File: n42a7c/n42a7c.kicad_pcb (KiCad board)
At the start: 2 copper layers, 265.5 x 105.1 mm, 111 parts, among them J1 Conn_01x02_Pin, J2 Conn_01x02_Pin, SW1 CPG151101S11-16, SW10 CPG151101S11-16, SW11 CPG151101S11-16, SW12 CPG151101S11-16, SW13 CPG151101S11-16, SW14 CPG151101S11-16, SW15 CPG151101S11-16, SW16 CPG151101S11-16, SW17 CPG151101S11-16, SW18 CPG151101S11-16, SW19 CPG151101S11-16, SW2 CPG151101S11-16, SW20 CPG151101S11-16, SW21 CPG151101S11-16, SW22 CPG151101S11-16, SW23 CPG151101S11-16, SW24 CPG151101S11-16, SW25 CPG151101S11-16, SW26 CPG151101S11-16, SW27 CPG151101S11-16, SW28 CPG151101S11-16, SW29 CPG151101S11-16, SW3 CPG151101S11-16, SW30 CPG151101S11-16, SW31 CPG151101S11-16, SW32 CPG151101S11-16, SW33 CPG151101S11-16, SW34 CPG151101S11-16, SW35 CPG151101S11-16, SW36 CPG151101S11-16, SW37 CPG151101S11-16, SW38 CPG151101S11-16, SW39 CPG151101S11-16, SW4 CPG151101S11-16, SW40 CPG151101S11-16, SW41 CPG151101S11-16, SW42 CPG151101S11-16, SW5 CPG151101S11-16, SW6 CPG151101S11-16, SW7 CPG151101S11-16, SW8 CPG151101S11-16, SW9 CPG151101S11-16, U1 XIAO-nRF52840-SMD

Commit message: revise switch pos.
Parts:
- moved SW_HPWR1 4.80 mm to (192.6, 24.4)
- moved SW_HPWR2 4.80 mm to (192.6, 24.4)
- moved J2 3.12 mm to (183.4, 31.6)
- moved SW_SPWR1 2.99 mm to (182.2, 27.1)
- moved DI4 1.19 mm to (270.3, 69.1)
- moved DS2 1.19 mm to (270.3, 42.9)
- moved DS4 1.19 mm to (270.3, 61.9)
- moved DI2 1.19 mm to (270.3, 50.0)
- moved J1 0.30 mm to (183.4, 38.8)
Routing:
- net Net-(J1-Pin_1): track 34.4 -> 43.6 mm
- net BAT+: track 61.5 -> 65.0 mm
- net IO 7: track 356.1 -> 353.7 mm
- net PWR: track 20.8 -> 22.4 mm
- net BAT-: track 45.6 -> 47.0 mm
- net IO 6: track 361.7 -> 360.5 mm
- net Net-(D19-K): track 107.9 -> 106.7 mm
- net Net-(D10-K): track 115.4 -> 114.2 mm
- net IO 5: track 386.6 -> 385.6 mm
- net IO 3: track 297.5 -> 296.7 mm
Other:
- outline, holes or cut-outs redrawn

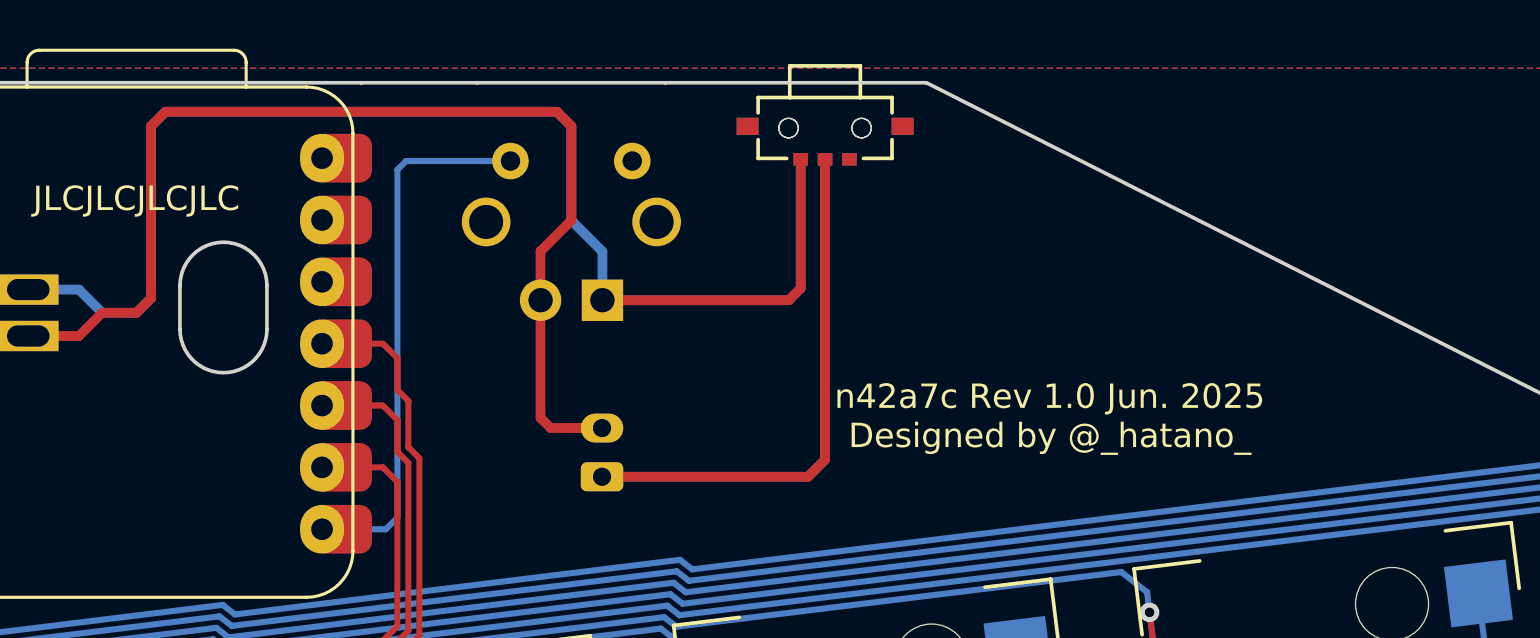
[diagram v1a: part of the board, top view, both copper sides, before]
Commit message: revise power connector
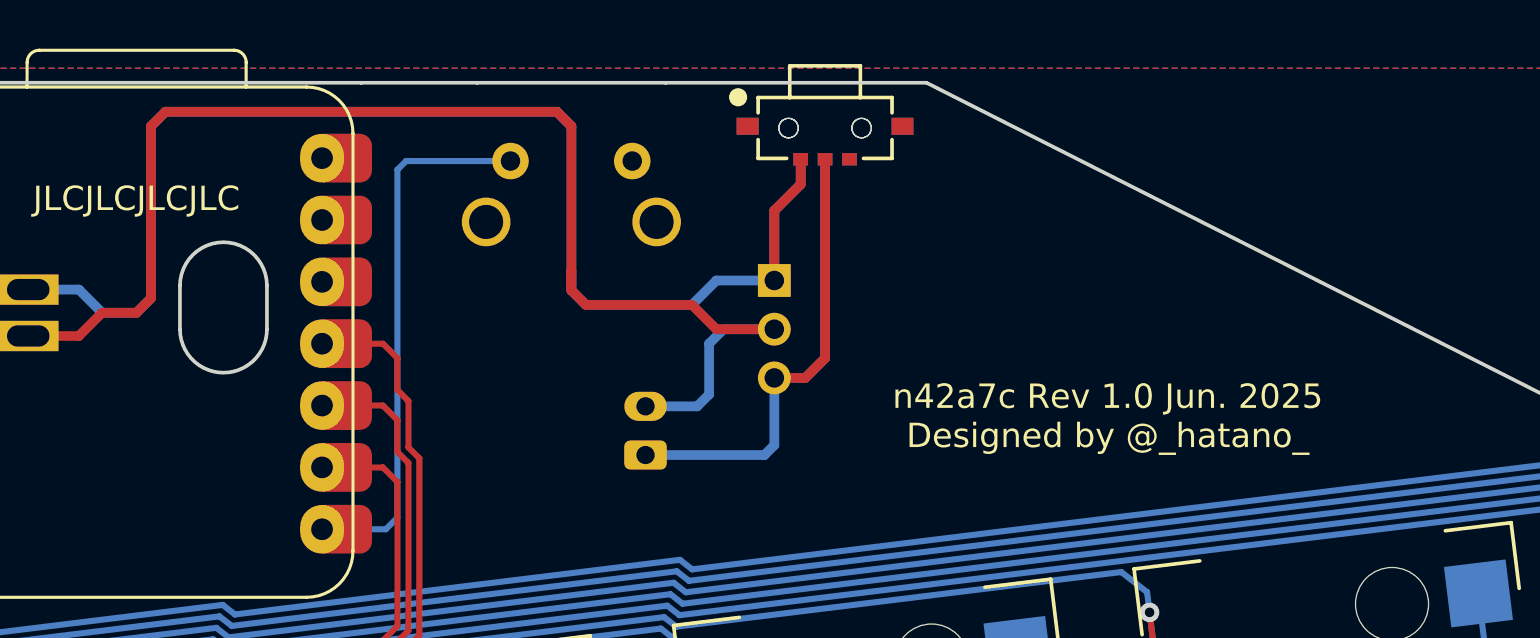
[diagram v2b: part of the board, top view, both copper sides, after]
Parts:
- J1: value Conn_01x02_Pin -> Conn_01x02
- J2: value Conn_01x02_Pin -> Conn_01x03; footprint Connector_PinHeader_2.54mm:PinHeader_1x02_P2.54mm_Vertical -> Connector_PinHeader_2.00mm:PinHeader_1x03_P2.00mm_Vertical
- SW_SPWR1: moved to B.Cu
- moved J2 7.11 mm to (190.5, 30.7), turned to 180 degrees
- moved J1 2.00 mm to (185.2, 37.9)
- turned SW_SPWR1 to 180 degrees
- renumbered SW_HPWR2 to SW_HPWR1, SW_HPWR1 to SW_HPWR2
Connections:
- SW_SPWR1 pad 1: PWR -> GND
- SW_SPWR1 pad 2: GND -> PWR
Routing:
- net Net-(J1-Pin_1): track 43.6 -> 29.4 mm
- net BAT+: track 65.0 -> 56.6 mm
- net BAT-: track 47.0 -> 54.9 mm
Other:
- board text added: "-"
- board text added: "C"

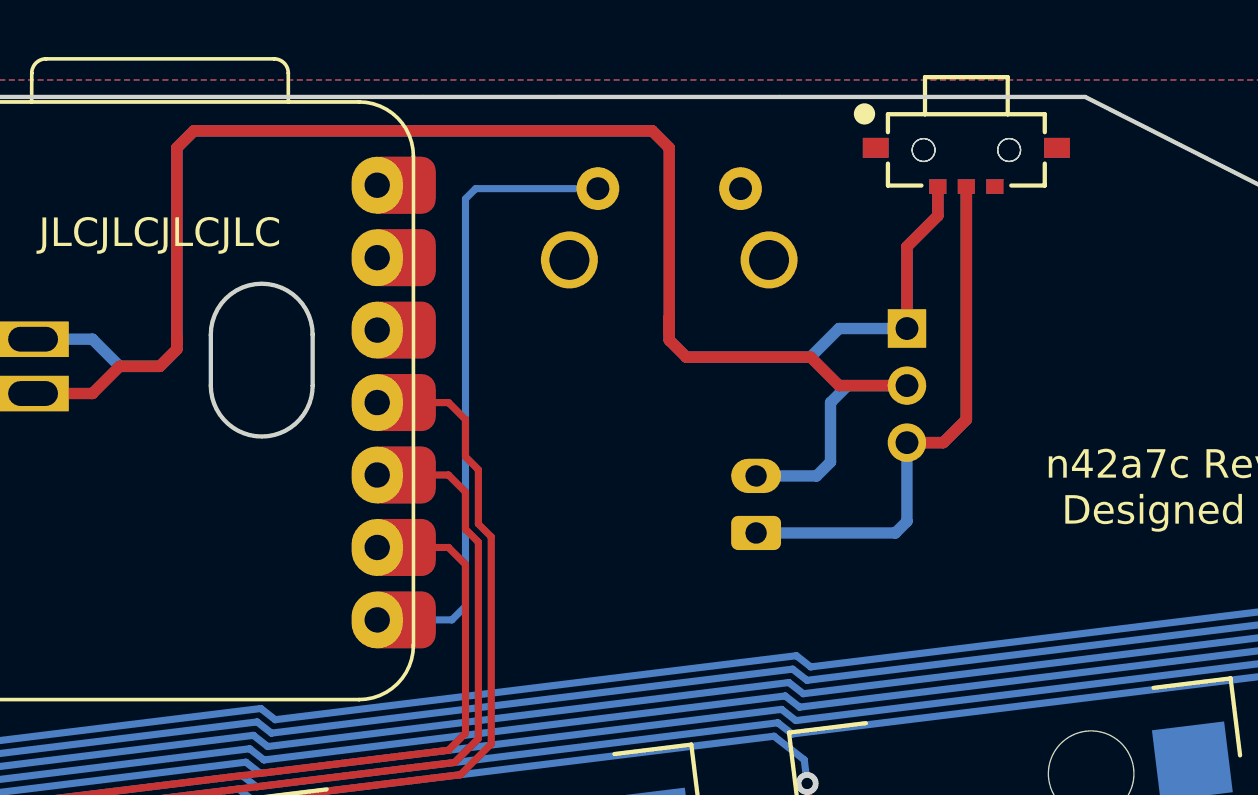
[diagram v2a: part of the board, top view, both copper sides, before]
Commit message: revise power SW
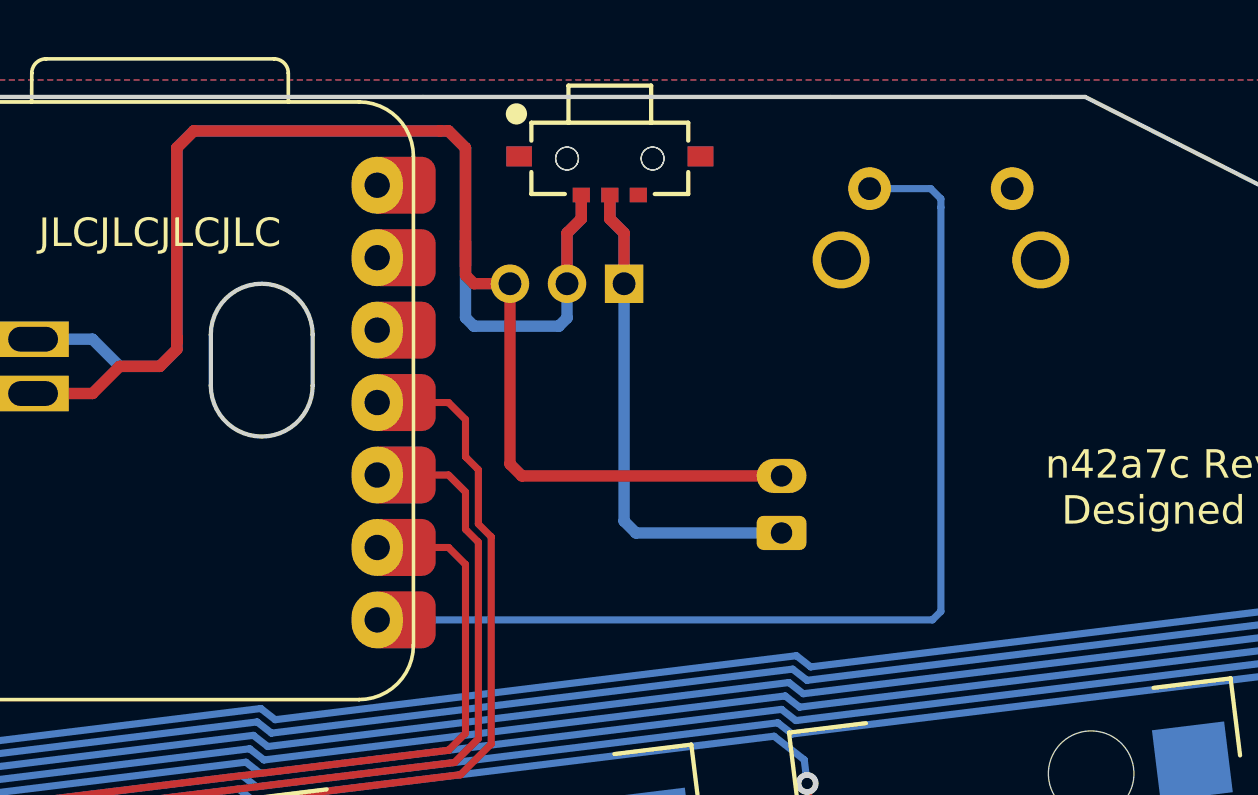
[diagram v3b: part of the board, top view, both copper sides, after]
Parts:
- moved SW_HPWR1 12.5 mm to (180.1, 24.7)
- moved SW_HPWR2 12.5 mm to (180.1, 24.7)
- moved J2 10.0 mm to (180.6, 29.2), turned to 90 degrees
- moved SW_SPWR1 9.52 mm to (191.7, 27.1)
- moved J1 0.89 mm to (186.1, 37.9)
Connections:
- J2 pad 1: BAT+ -> Net-(J1-Pin_1)
- J2 pad 2: BAT- -> BAT+
- J2 pad 3: Net-(J1-Pin_1) -> BAT-
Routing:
- net BAT+: track 56.6 -> 41.3 mm
- net PWR: track 22.4 -> 37.0 mm
- net Net-(J1-Pin_1): track 29.4 -> 20.7 mm
- net BAT-: track 54.9 -> 46.6 mm
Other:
- outline, holes or cut-outs redrawn

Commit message: revise switch
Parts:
- removed SW_HPWR2: SSAJ110100, cscslib:SSAJ110100
- J2: footprint Connector_PinHeader_2.00mm:PinHeader_1x03_P2.00mm_Vertical -> Connector_PinHeader_2.00mm:PinHeader_1x04_P2.00mm_Vertical
- SW_HPWR1: value SSAJ110100 -> SK-12D11; footprint cscslib:SSAJ110100 -> cscslib:SK-12D11; moved to B.Cu
- SW_SPWR1: value SW_SPWR -> THAU13-AB-R
- moved J2 1.91 mm to (182.3, 30.1)
- moved SW_HPWR1 1.23 mm to (181.3, 25.0)
- moved J1 0.89 mm to (186.1, 37.0)
- moved SW_SPWR1 0.30 mm to (192.0, 27.1)
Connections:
- J2 pad 2: BAT+ -> BAT-
- J2 pad 3: BAT- -> BAT+
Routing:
- net Net-(J1-Pin_1): track 20.7 -> 16.0 mm
- net BAT-: track 46.6 -> 50.4 mm
- net BAT+: track 41.3 -> 39.5 mm
- net PWR: track 37.0 -> 36.0 mm
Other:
- outline, holes or cut-outs redrawn
